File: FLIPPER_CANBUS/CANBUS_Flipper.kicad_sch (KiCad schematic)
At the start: 23 parts, among them J1 Conn_01x08_Socket, J2 Conn_01x10_Socket, J3 Conn, U3 MCP251863T-H-SS, Y1 40MHz

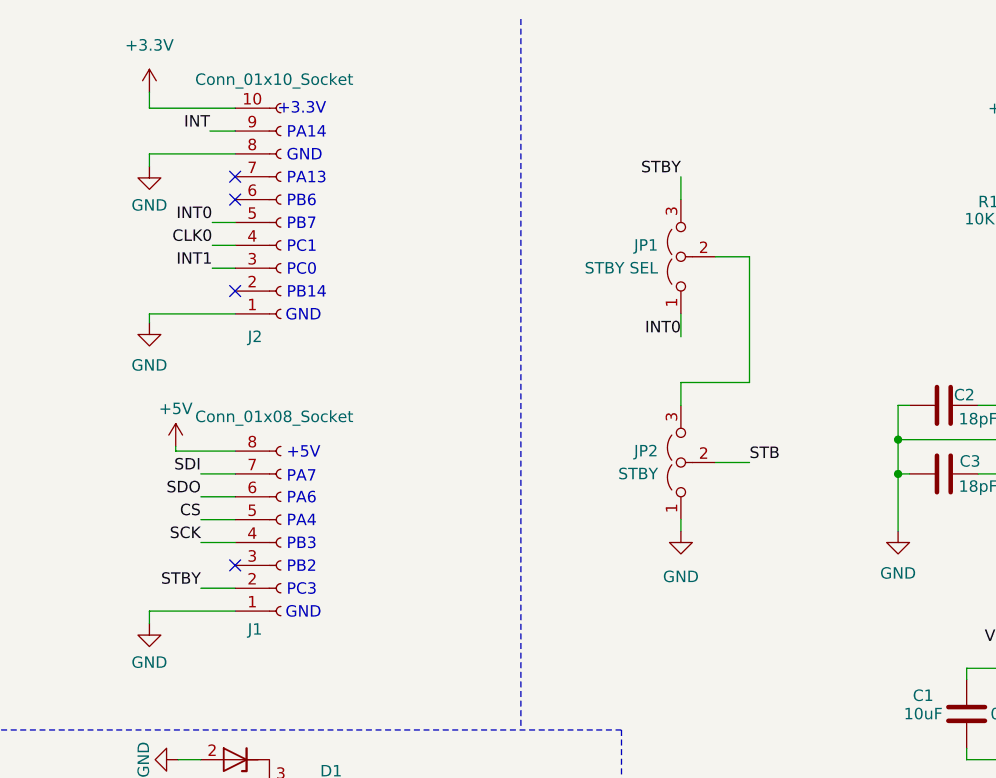
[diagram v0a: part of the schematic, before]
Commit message: feat(Hw):Update_Schematic_Route_And_Labels
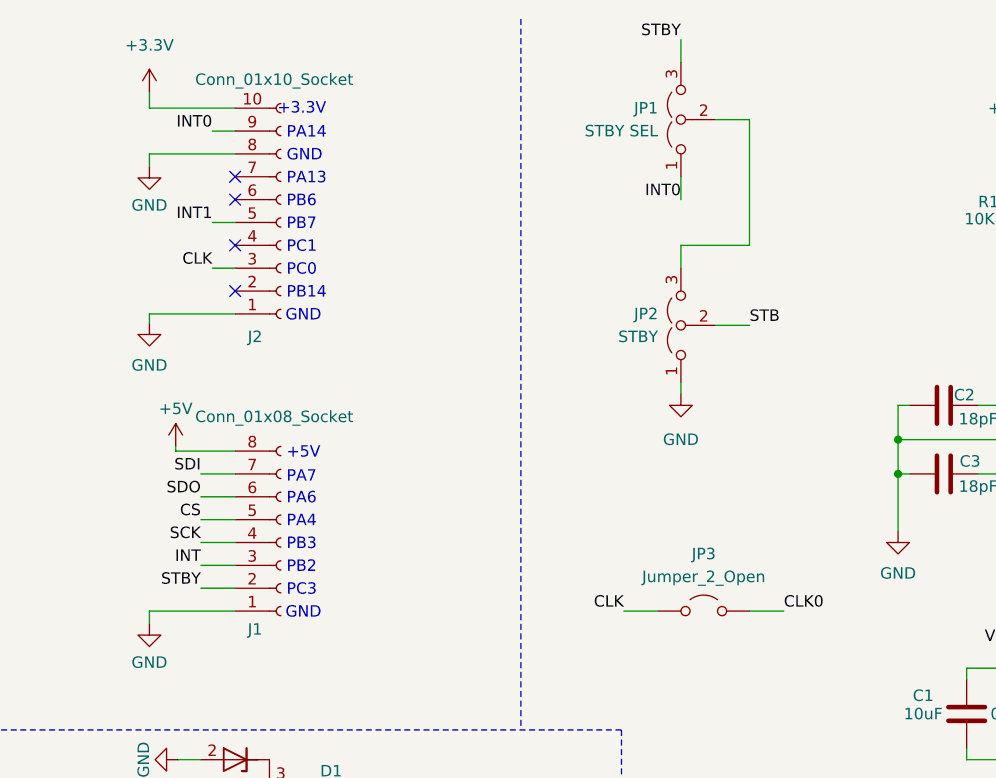
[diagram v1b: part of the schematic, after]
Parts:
- added JP3: Jumper_2_Open, Jumper:SolderJumper-2_P1.3mm_Open_Pad1.0x1.5mm, symbol Jumper:Jumper_2_Open
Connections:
- net CLK0: now also JP3.2 (B); no longer J2.4 (Pin_4)
- net INT: now also J1.3 (Pin_3); no longer J2.9 (Pin_9)
- net INT0: now also J2.9 (Pin_9); no longer J2.5 (Pin_5)
- net INT1: now also J2.5 (Pin_5); no longer J2.3 (Pin_3)
- new net CLK: J2.3 (Pin_3), JP3.1 (A)
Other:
- moved on the sheet: JP1, JP2
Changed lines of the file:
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@@
 	)
 	(no_connect
-		(at 46.99 73.66)
-	)
-	(no_connect
 		(at 46.99 33.02)
 	)
@@
 		(at 46.99 43.18)
 	)
+	(no_connect
+		(at 46.99 38.1)
+	)
 	(wire
 		(pts
@@
 	(wire
 		(pts
-			(xy 96.52 69.85) (xy 96.52 68.58)
+			(xy 96.52 54.61) (xy 96.52 53.34)
 		)
 		(stroke
@@
 	(wire
 		(pts
-			(xy 96.52 53.34) (xy 96.52 55.88)
+			(xy 96.52 38.1) (xy 96.52 40.64)
 		)
 		(stroke
@@
 	(wire
 		(pts
-			(xy 104.14 53.34) (xy 96.52 53.34)
+			(xy 104.14 38.1) (xy 96.52 38.1)
 		)
 		(stroke
@@
 	(wire
 		(pts
-			(xy 100.33 39.37) (xy 104.14 39.37)
+			(xy 100.33 24.13) (xy 104.14 24.13)
 		)
 		(stroke
@@
 	(wire
 		(pts
-			(xy 44.45 38.1) (xy 46.99 38.1)
-		)
-		(stroke
-			(width 0)
-			(type default)
-		)
-	)
-	(wire
-		(pts
 			(xy 43.18 71.12) (xy 46.99 71.12)
 		)
@@
 	(wire
 		(pts
+			(xy 90.17 78.74) (xy 93.98 78.74)
+		)
+		(stroke
+			(width 0)
+			(type default)
+		)
+	)
+	(wire
+		(pts
 			(xy 43.18 100.33) (xy 41.91 100.33)
 		)
@@
 	(wire
 		(pts
-			(xy 96.52 48.26) (xy 96.52 45.72)
+			(xy 96.52 33.02) (xy 96.52 30.48)
 		)
 		(stroke
@@
 	(wire
 		(pts
+			(xy 44.45 25.4) (xy 46.99 25.4)
+		)
+		(stroke
+			(width 0)
+			(type default)
+		)
+	)
+	(wire
+		(pts
 			(xy 165.1 67.31) (xy 166.37 67.31)
 		)
@@
 	(wire
 		(pts
-			(xy 24.13 123.19) (xy 24.13 125.73)
+			(xy 107.95 78.74) (xy 104.14 78.74)
 		)
 		(stroke
@@
 	(wire
 		(pts
-			(xy 147.32 38.1) (xy 151.13 38.1)
+			(xy 24.13 123.19) (xy 24.13 125.73)
 		)
 		(stroke
@@
 	(wire
 		(pts
-			(xy 54.61 114.3) (xy 52.07 114.3)
+			(xy 147.32 38.1) (xy 151.13 38.1)
 		)
 		(stroke
@@
 	(wire
 		(pts
-			(xy 146.939 60.96) (xy 151.13 60.96)
+			(xy 54.61 114.3) (xy 52.07 114.3)
 		)
 		(stroke
@@
 	(wire
 		(pts
-			(xy 24.13 114.3) (xy 24.13 115.57)
+			(xy 146.939 60.96) (xy 151.13 60.96)
 		)
 		(stroke
@@
 	(wire
 		(pts
-			(xy 163.83 19.05) (xy 163.83 22.86)
+			(xy 24.13 114.3) (xy 24.13 115.57)
 		)
 		(stroke
@@
 	(wire
 		(pts
-			(xy 181.61 48.26) (xy 186.69 48.26)
+			(xy 163.83 19.05) (xy 163.83 22.86)
 		)
 		(stroke
@@
 	(wire
 		(pts
-			(xy 44.196 25.4) (xy 46.99 25.4)
+			(xy 181.61 48.26) (xy 186.69 48.26)
 		)
 		(stroke
@@
 	(wire
 		(pts
-			(xy 104.14 62.23) (xy 100.33 62.23)
+			(xy 104.14 46.99) (xy 100.33 46.99)
 		)
 		(stroke
@@
 	(wire
 		(pts
-			(xy 104.14 39.37) (xy 104.14 53.34)
+			(xy 104.14 24.13) (xy 104.14 38.1)
 		)
 		(stroke
@@
 	(wire
 		(pts
-			(xy 96.52 30.48) (xy 96.52 33.02)
+			(xy 43.18 73.66) (xy 46.99 73.66)
+		)
+		(stroke
+			(width 0)
+			(type default)
+		)
+	)
+	(wire
+		(pts
+			(xy 96.52 15.24) (xy 96.52 17.78)
 		)
 		(stroke
@@
 	)
 	(label "STBY"
-		(at 96.52 30.48 180)
+		(at 96.52 15.24 180)
 		(effects
 			(font
@@
 	)
 	(label "INT0"
-		(at 96.52 48.26 180)
+		(at 96.52 33.02 180)
 		(effects
 			(font
@@
 		)
 	)
+	(label "CLK"
+		(at 90.17 78.74 180)
+		(effects
+			(font
+				(size 1.27 1.27)
+			)
+			(justify right bottom)
+		)
+	)
 	(label "SDI"
 		(at 43.18 63.5 180)
@@
 	)
 	(label "INT"
-		(at 44.196 25.4 180)
+		(at 43.18 73.66 180)
 		(effects
 			(font
@@
 	)
 	(label "STB"
-		(at 104.14 62.23 0)
+		(at 104.14 46.99 0)
 		(effects
 			(font
@@
 		)
 	)
-	(label "CLK0"
-		(at 44.45 38.1 180)
+	(label "CLK"
+		(at 44.45 40.64 180)
 		(effects
 			(font
@@
 	)
 	(label "INT1"
-		(at 44.45 40.64 180)
+		(at 44.45 35.56 180)
 		(effects
 			(font
@@
 	)
 	(label "INT0"
-		(at 44.45 35.56 180)
+		(at 44.45 25.4 180)
 		(effects
 			(font
@@
 		)
 	)
+	(label "CLK0"
+		(at 107.95 78.74 0)
+		(effects
+			(font
+				(size 1.27 1.27)
+			)
+			(justify left bottom)
+		)
+	)
 	(label "INT0"
 		(at 147.32 50.8 180)
@@
 	)
 	(symbol
+		(lib_id "Jumper:Jumper_2_Open")
+		(at 99.06 78.74 0)
+		(unit 1)
+		(exclude_from_sim no)
+		(in_bom yes)
+		(on_board yes)
+		(dnp no)
+		(property "Reference" "JP3"
+			(at 99.06 72.39 0)
+			(effects
+				(font
+					(size 1.27 1.27)
+				)
+			)
+		)
+		(property "Value" "Jumper_2_Open"
+			(at 99.06 74.93 0)
+			(effects
+				(font
+					(size 1.27 1.27)
+				)
+			)
+		)
+		(property "Footprint" "Jumper:SolderJumper-2_P1.3mm_Open_Pad1.0x1.5mm"
+			(at 99.06 78.74 0)
+			(effects
+				(font
+					(size 1.27 1.27)
+				)
+				(hide yes)
+			)
+		)
+		(property "Datasheet" "~"
+			(at 99.06 78.74 0)
+			(effects
+				(font
+					(size 1.27 1.27)
+				)
+				(hide yes)
+			)
+		)
+		(property "Description" "Jumper, 2-pole, open"
+			(at 99.06 78.74 0)
+			(effects
+				(font
+					(size 1.27 1.27)
+				)
+				(hide yes)
+			)
+		)
+		(pin "2"
+		)
+		(pin "1"
+		)
+		(instances
+			(project ""
+				(path "/8c23e026-b908-4d4a-84cd-fb733847c38f"
+					(reference "JP3")
+					(unit 1)
+				)
+			)
+		)
+	)
+	(symbol
 		(lib_id "Diode:MMBZxx")
 		(at 46.99 97.79 270)
@@
 	(symbol
 		(lib_id "Jumper:Jumper_3_Open")
-		(at 96.52 39.37 90)
+		(at 96.52 24.13 90)
 		(unit 1)
 		(exclude_from_sim no)
@@
 		(fields_autoplaced yes)
 		(property "Reference" "JP1"
-			(at 93.98 38.0999 90)
+			(at 93.98 22.8599 90)
 			(effects
 				(font
@@
 		)
 		(property "Value" "STBY SEL"
-			(at 93.98 40.6399 90)
+			(at 93.98 25.3999 90)
 			(effects
 				(font
@@
 		)
 		(property "Footprint" "Footprints:Jumper"
-			(at 96.52 39.37 0)
+			(at 96.52 24.13 0)
 			(effects
 				(font
@@
 		)
 		(property "Datasheet" "~"
-			(at 96.52 39.37 0)
+			(at 96.52 24.13 0)
 			(effects
 				(font
@@
 		)
 		(property "Description" "Jumper, 3-pole, both open"
-			(at 96.52 39.37 0)
+			(at 96.52 24.13 0)
 			(effects
 				(font
@@
 		(lib_name "GND_1")
 		(lib_id "power:GND")
-		(at 96.52 69.85 0)
+		(at 96.52 54.61 0)
 		(unit 1)
 		(exclude_from_sim no)
@@
 		(fields_autoplaced yes)
 		(property "Reference" "#PWR015"
-			(at 96.52 76.2 0)
+			(at 96.52 60.96 0)
 			(effects
 				(font
@@
 		)
 		(property "Value" "GND"
-			(at 96.52 74.93 0)
+			(at 96.52 59.69 0)
 			(effects
 				(font
@@
 		)
 		(property "Footprint" ""
-			(at 96.52 69.85 0)
+			(at 96.52 54.61 0)
 			(effects
 				(font
@@
 		)
 		(property "Datasheet" ""
-			(at 96.52 69.85 0)
+			(at 96.52 54.61 0)
 			(effects
 				(font
@@
 		)
 		(property "Description" "Power symbol creates a global label with name \"GND\" , ground"
-			(at 96.52 69.85 0)
+			(at 96.52 54.61 0)
 			(effects
 				(font
@@
 	(symbol
 		(lib_id "Jumper:Jumper_3_Open")
-		(at 96.52 62.23 90)
+		(at 96.52 46.99 90)
 		(unit 1)
 		(exclude_from_sim no)
@@
 		(fields_autoplaced yes)
 		(property "Reference" "JP2"
-			(at 93.98 60.9599 90)
+			(at 93.98 45.7199 90)
 			(effects
 				(font
@@
 		)
 		(property "Value" "STBY"
-			(at 93.98 63.4999 90)
+			(at 93.98 48.2599 90)
 			(effects
 				(font
@@
 		)
 		(property "Footprint" "Footprints:Jumper"
-			(at 96.52 62.23 0)
+			(at 96.52 46.99 0)
 			(effects
 				(font
@@
 		)
 		(property "Datasheet" "~"
-			(at 96.52 62.23 0)
+			(at 96.52 46.99 0)
 			(effects
 				(font
@@
 		)
 		(property "Description" "Jumper, 3-pole, both open"
-			(at 96.52 62.23 0)
+			(at 96.52 46.99 0)
 			(effects
 				(font

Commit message: feat(Hw):Update_Schematic
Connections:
- net CLK renamed CLKO
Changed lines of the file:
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@@
 		)
 	)
-	(label "CLK"
+	(label "CLKO"
 		(at 90.17 78.74 180)
 		(effects
@@
 		)
 	)
-	(label "CLK"
+	(label "CLKO"
 		(at 44.45 40.64 180)
 		(effects

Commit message: feat(Hw):Update_BOM
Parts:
- J3: Proveedor (none) -> STEREN; manf# (none) -> TRT-02
- JP1, JP2: LCSC# (none) -> C163836
- JP3: now not fitted
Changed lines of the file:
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@@
 			)
 		)
+		(property "Proveedor" ""
+			(at 163.83 90.17 0)
+			(effects
+				(font
+					(size 1.27 1.27)
+				)
+				(hide yes)
+			)
+		)
 		(pin "1"
 		)
@@
 			)
 		)
+		(property "Proveedor" ""
+			(at 138.43 90.17 0)
+			(effects
+				(font
+					(size 1.27 1.27)
+				)
+				(hide yes)
+			)
+		)
 		(pin "1"
 		)
@@
 			)
 		)
+		(property "Proveedor" ""
+			(at 133.35 34.29 0)
+			(effects
+				(font
+					(size 1.27 1.27)
+				)
+				(hide yes)
+			)
+		)
 		(pin "2"
 		)
@@
 			)
 		)
+		(property "Proveedor" ""
+			(at 46.99 130.81 90)
+			(effects
+				(font
+					(size 1.27 1.27)
+				)
+				(hide yes)
+			)
+		)
 		(pin "2"
 		)
@@
 			)
 		)
+		(property "Proveedor" ""
+			(at 128.27 90.17 0)
+			(effects
+				(font
+					(size 1.27 1.27)
+				)
+				(hide yes)
+			)
+		)
 		(pin "2"
 		)
@@
 			)
 		)
+		(property "Proveedor" ""
+			(at 125.73 55.88 90)
+			(effects
+				(font
+					(size 1.27 1.27)
+				)
+				(hide yes)
+			)
+		)
 		(pin "2"
 		)
@@
 			)
 		)
+		(property "Proveedor" ""
+			(at 166.37 45.72 0)
+			(effects
+				(font
+					(size 1.27 1.27)
+				)
+				(hide yes)
+			)
+		)
 		(pin "7"
 		)
@@
 			)
 		)
+		(property "Proveedor" ""
+			(at 125.73 63.5 90)
+			(effects
+				(font
+					(size 1.27 1.27)
+				)
+				(hide yes)
+			)
+		)
 		(pin "1"
 		)
@@
 		(in_bom yes)
 		(on_board yes)
-		(dnp no)
+		(dnp yes)
 		(property "Reference" "JP3"
 			(at 99.06 72.39 0)
@@
 			)
 		)
+		(property "Proveedor" ""
+			(at 99.06 78.74 0)
+			(effects
+				(font
+					(size 1.27 1.27)
+				)
+				(hide yes)
+			)
+		)
 		(pin "2"
 		)
@@
 			)
 		)
+		(property "Proveedor" ""
+			(at 46.99 97.79 90)
+			(effects
+				(font
+					(size 1.27 1.27)
+				)
+				(hide yes)
+			)
+		)
 		(pin "2"
 		)
@@
 			)
 		)
+		(property "Proveedor" ""
+			(at 189.23 90.17 0)
+			(effects
+				(font
+					(size 1.27 1.27)
+				)
+				(hide yes)
+			)
+		)
 		(pin "1"
 		)
@@
 			)
 		)
+		(property "Proveedor" ""
+			(at 33.02 114.3 90)
+			(effects
+				(font
+					(size 1.27 1.27)
+				)
+				(hide yes)
+			)
+		)
 		(pin "2"
 		)
@@
 			)
 		)
+		(property "Proveedor" ""
+			(at 24.13 119.38 0)
+			(effects
+				(font
+					(size 1.27 1.27)
+				)
+				(hide yes)
+			)
+		)
 		(pin "2"
 		)
@@
 			)
 		)
+		(property "Proveedor" ""
+			(at 137.16 59.69 90)
+			(effects
+				(font
+					(size 1.27 1.27)
+				)
+				(hide yes)
+			)
+		)
 		(pin "1"
 		)
@@
 			)
 		)
+		(property "Proveedor" ""
+			(at 52.07 35.56 0)
+			(effects
+				(font
+					(size 1.27 1.27)
+				)
+				(hide yes)
+			)
+		)
 		(pin "1"
 		)
@@
 			)
 		)
+		(property "Proveedor" ""
+			(at 179.07 90.17 0)
+			(effects
+				(font
+					(size 1.27 1.27)
+				)
+				(hide yes)
+			)
+		)
 		(pin "2"
 		)
@@
 			)
 		)
+		(property "Proveedor" ""
+			(at 52.07 109.22 0)
+			(effects
+				(font
+					(size 1.27 1.27)
+				)
+				(hide yes)
+			)
+		)
 		(pin "1"
 		)
@@
 			)
 		)
+		(property "LCSC#" "C163836"
+			(at 96.52 24.13 90)
+			(effects
+				(font
+					(size 1.27 1.27)
+				)
+				(hide yes)
+			)
+		)
+		(property "Proveedor" ""
+			(at 96.52 24.13 90)
+			(effects
+				(font
+					(size 1.27 1.27)
+				)
+				(hide yes)
+			)
+		)
 		(pin "1"
 		)
@@
 			)
 		)
+		(property "Proveedor" ""
+			(at 153.67 90.17 0)
+			(effects
+				(font
+					(size 1.27 1.27)
+				)
+				(hide yes)
+			)
+		)
 		(pin "2"
 		)
@@
 			)
 		)
+		(property "Proveedor" ""
+			(at 52.07 71.12 0)
+			(effects
+				(font
+					(size 1.27 1.27)
+				)
+				(hide yes)
+			)
+		)
 		(pin "6"
 		)
@@
 			)
 		)
+		(property "Proveedor" ""
+			(at 24.13 109.22 0)
+			(effects
+				(font
+					(size 1.27 1.27)
+				)
+				(hide yes)
+			)
+		)
 		(pin "2"
 		)
@@
 			)
 		)
+		(property "Proveedor" ""
+			(at 52.07 119.38 0)
+			(effects
+				(font
+					(size 1.27 1.27)
+				)
+				(hide yes)
+			)
+		)
 		(pin "1"
 		)
@@
 			)
 		)
+		(property "LCSC#" "C163836"
+			(at 96.52 46.99 90)
+			(effects
+				(font
+					(size 1.27 1.27)
+				)
+				(hide yes)
+			)
+		)
+		(property "Proveedor" ""
+			(at 96.52 46.99 90)
+			(effects
+				(font
+					(size 1.27 1.27)
+				)
+				(hide yes)
+			)
+		)
 		(pin "1"
 		)
@@
 			)
 		)
-		(property "manf#" ""
+		(property "manf#" "TRT-02"
+			(at 77.47 113.03 0)
+			(effects
+				(font
+					(size 1.27 1.27)
+				)
+				(hide yes)
+			)
+		)
+		(property "Proveedor" "STEREN"
 			(at 77.47 113.03 0)
 			(effects
